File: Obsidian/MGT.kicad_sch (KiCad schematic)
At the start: 1 part, among them U1 XC7A35T-CSG325

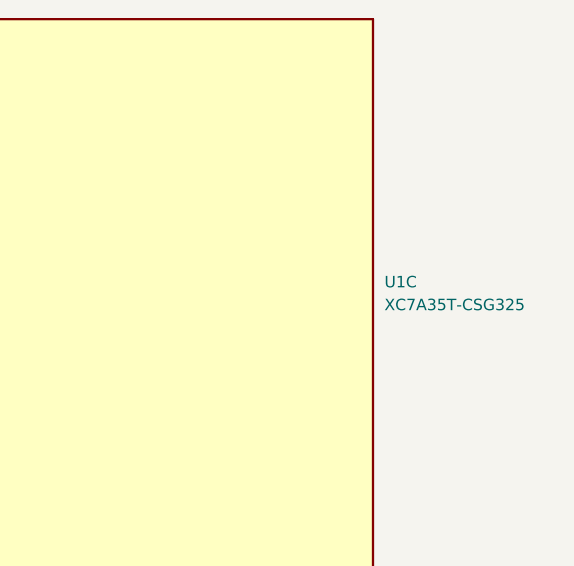
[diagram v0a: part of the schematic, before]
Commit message: Removing unnecessary components for the interface. Adding SPIN schematic and footprint
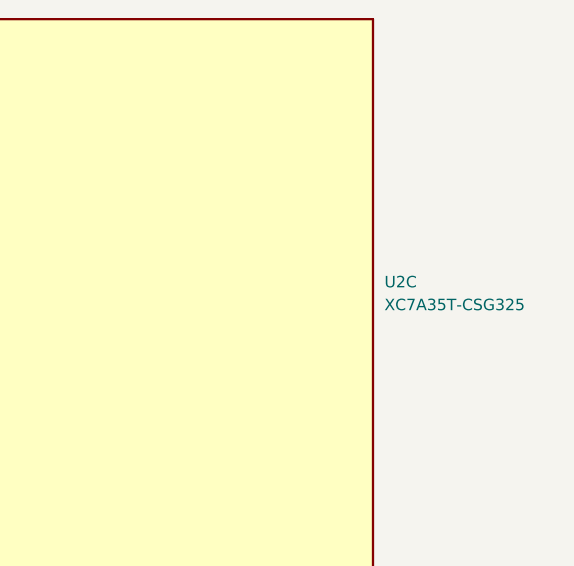
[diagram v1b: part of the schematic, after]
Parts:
- renumbered U1 to U2
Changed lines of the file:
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@@
 		(dnp no)
 		(fields_autoplaced yes)
-		(property "Reference" "U1"
+		(property "Reference" "U2"
 			(at 193.04 78.7399 0)
 			(effects
@@
 			(project "Marble_Tiny"
 				(path "/c2a4f786-b14c-434a-acf7-b20fb2221b0b/5109eb00-35d9-449a-bfa1-f3cdbf070d89"
-					(reference "U1")
+					(reference "U2")
 					(unit 3)
 				)
